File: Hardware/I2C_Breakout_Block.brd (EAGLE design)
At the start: 30.5 x 44.5 mm, 25 parts, among them U2 PCA9306

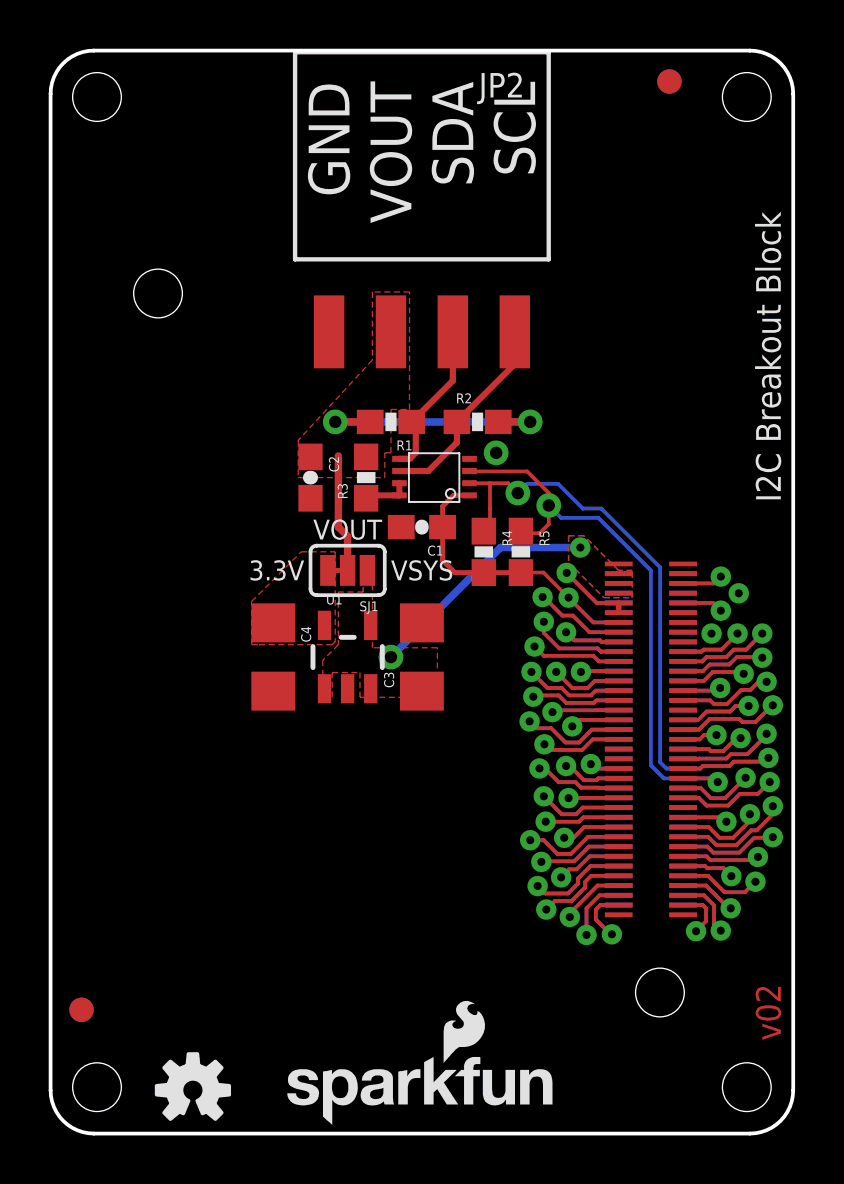
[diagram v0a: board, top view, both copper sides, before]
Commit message: Rev to 10, fix gnd/pwr/text
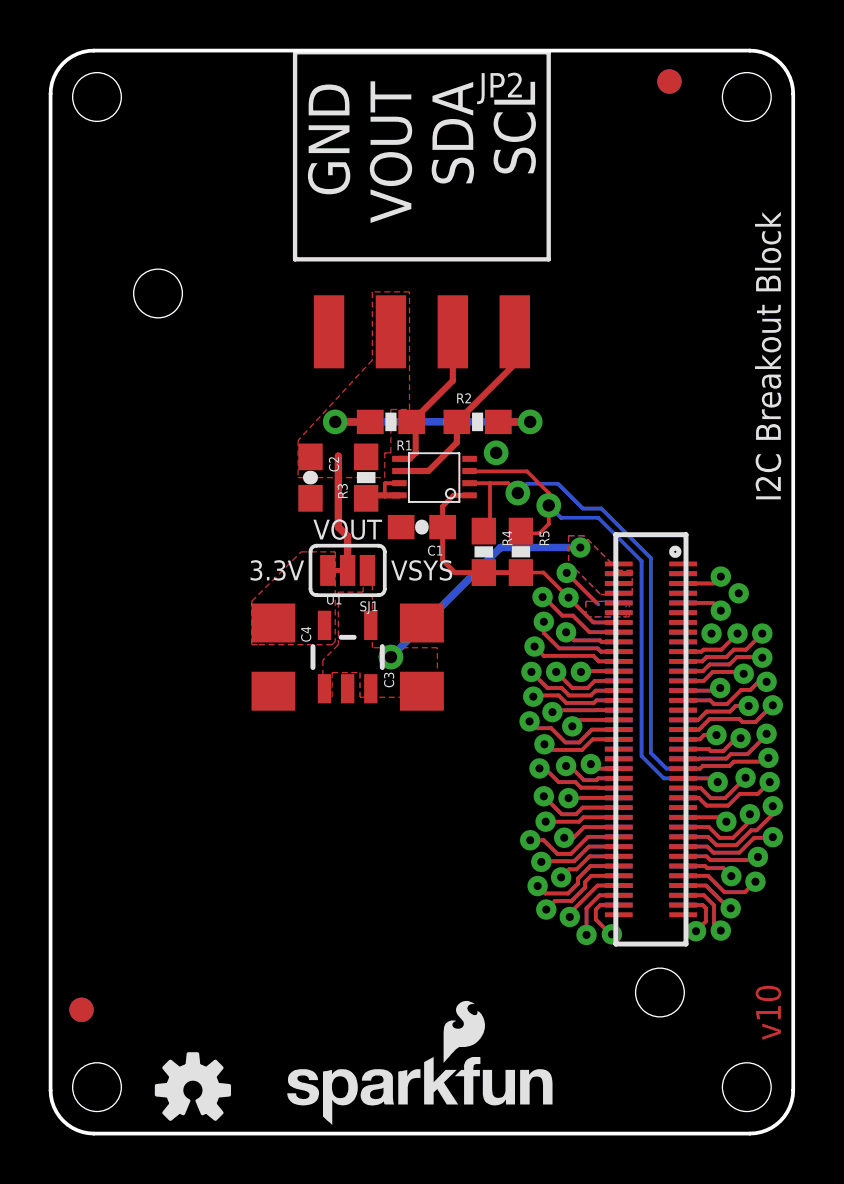
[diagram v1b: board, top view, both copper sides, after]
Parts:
- R1, R2: value 2.2k -> 10K
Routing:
- net 3.3V: track 6.49 -> 3.58 mm
- net N$1: track 1.91 -> 2.50 mm
- added copper zone on layer 1, net 3.3V
- added copper zone on layer 16, net 3.3V
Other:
- board text added: "v10"
- board text removed: "v02"

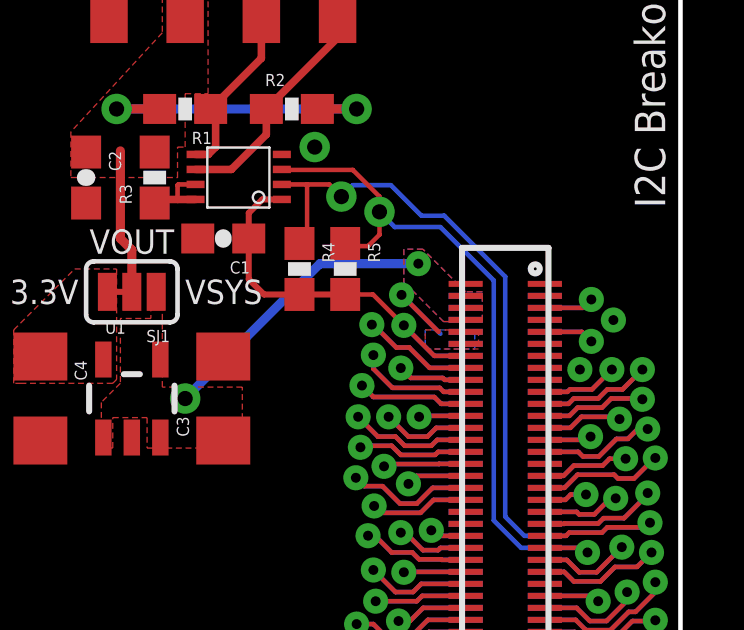
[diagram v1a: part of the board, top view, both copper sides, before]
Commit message: fixed airwire with Package update
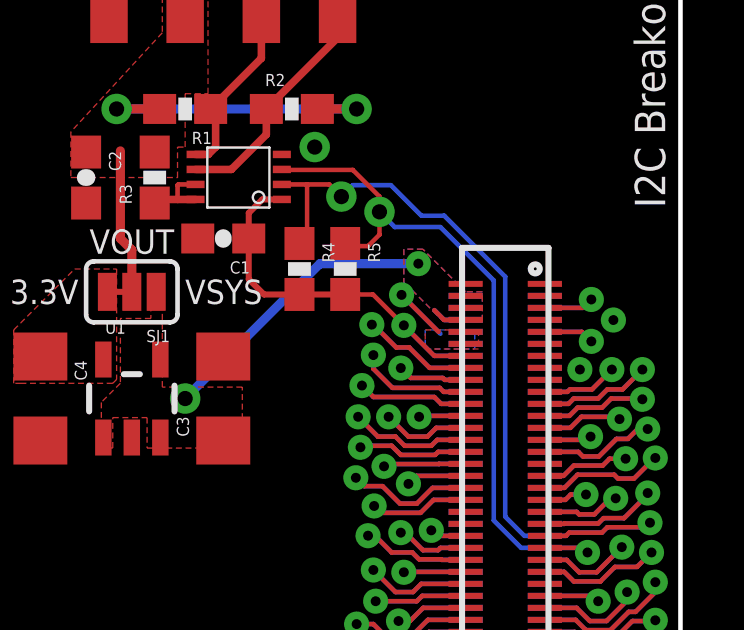
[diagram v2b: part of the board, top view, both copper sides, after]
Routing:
- net VSYS: track 9.76 -> 12.1 mm
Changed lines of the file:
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@@
 <setting verticaltext="up"/>
 </settings>
-<grid distance="0.05" unitdist="inch" unit="inch" style="lines" multiple="1" display="yes" altdistance="0.005" altunitdist="inch" altunit="inch"/>
+<grid distance="0.001" unitdist="inch" unit="inch" style="lines" multiple="1" display="yes" altdistance="0.005" altunitdist="inch" altunit="inch"/>
 <layers>
 <layer number="1" name="Top" color="4" fill="1" visible="yes" active="yes"/>
-<layer number="2" name="Route2" color="1" fill="3" visible="no" active="yes"/>
+<layer number="2" name="Route2" color="1" fill="3" visible="yes" active="yes"/>
 <layer number="15" name="Route15" color="4" fill="6" visible="no" active="yes"/>
-<layer number="16" name="Bottom" color="1" fill="1" visible="no" active="yes"/>
+<layer number="16" name="Bottom" color="1" fill="1" visible="yes" active="yes"/>
 <layer number="17" name="Pads" color="2" fill="1" visible="yes" active="yes"/>
 <layer number="18" name="Vias" color="2" fill="1" visible="yes" active="yes"/>
@@
 <vertex x="21.5392" y="23.1648"/>
 </polygon>
+<wire x1="23.32" y1="22.18" x2="22.6002" y2="22.18" width="0.1524" layer="16"/>
+<wire x1="22.6002" y1="22.18" x2="22.2758" y2="22.5044" width="0.1524" layer="16"/>
+<wire x1="23.32" y1="22.1798" x2="22.6004" y2="22.1798" width="0.1524" layer="1"/>
+<wire x1="22.6004" y1="22.1798" x2="22.2758" y2="22.5044" width="0.1524" layer="1"/>
 </signal>
 <signal name="3.3V">
